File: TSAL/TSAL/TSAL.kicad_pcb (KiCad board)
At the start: 2 copper layers, 56.5 x 34.3 mm, 16 parts, among them J1 Conn_01x02, J2 Conn_01x02, J3 Conn_01x02, J4 Conn_01x02, Q1 Q_NMOS_GDS, U1 LTV-817S, U2 LM555xM

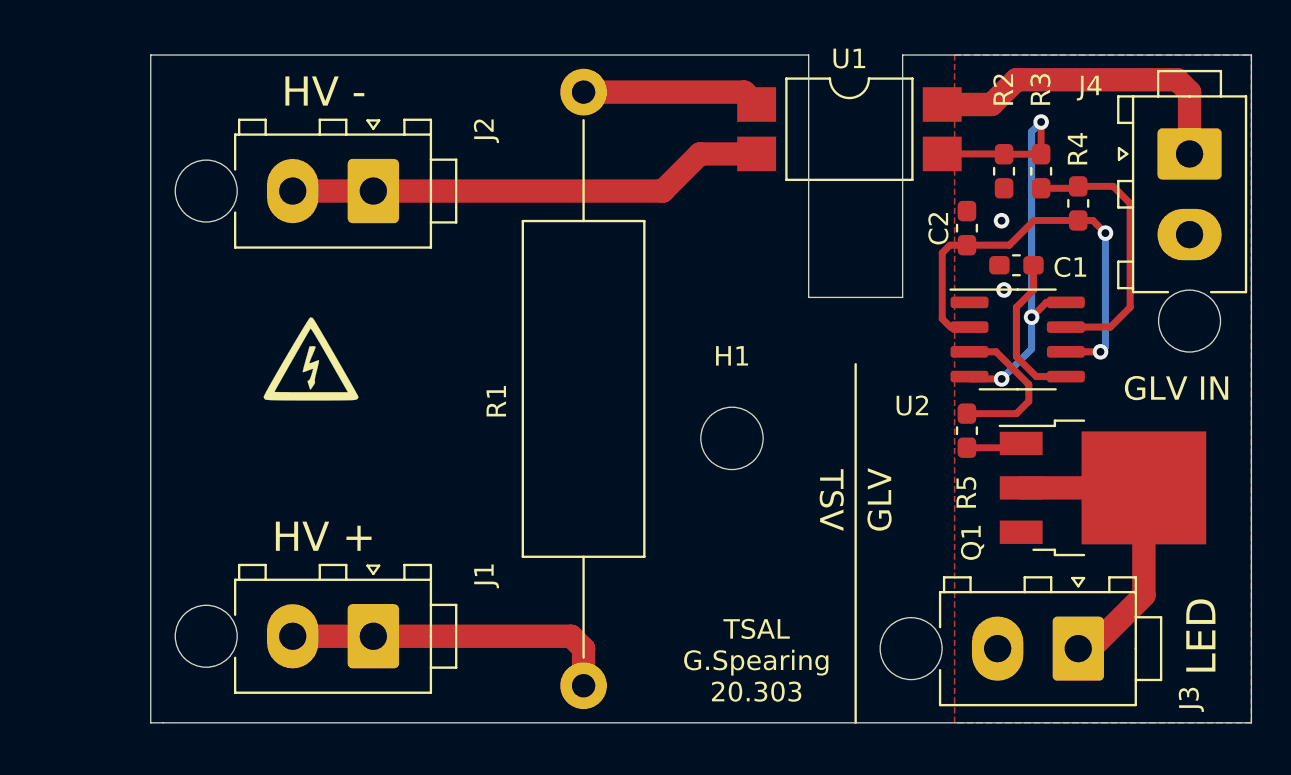
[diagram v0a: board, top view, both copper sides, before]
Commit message: change to CC driver
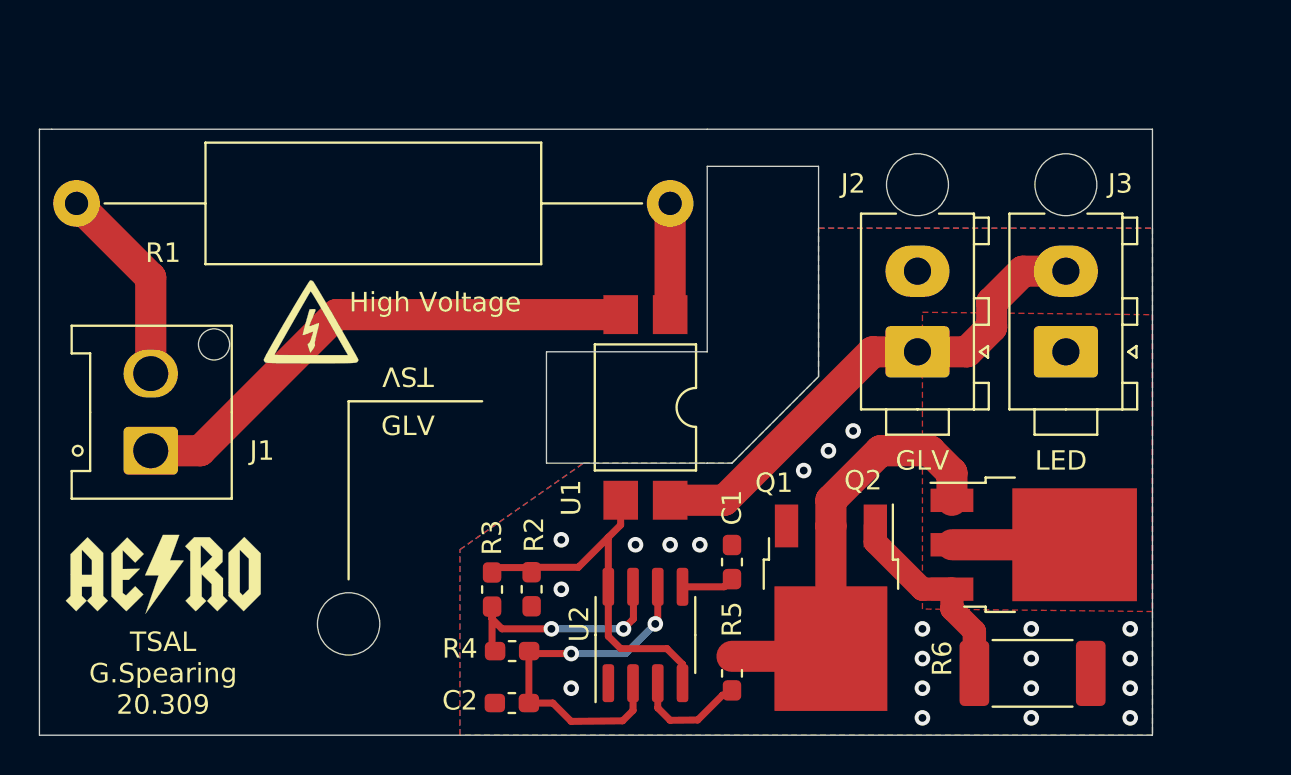
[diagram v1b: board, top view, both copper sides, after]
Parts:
- removed J4: Conn_01x02, Connector_TE-Connectivity:TE_MATE-N-LOK_1-770866-x_1x02_P4.14mm_Vertical
- added G***: LOGO, AERO_CUSTOM:AERO_Logo_10x4mm, F.Cu at (132.7, 90.2)
- added Q2: 040N03LG, Package_TO_SOT_SMD:TO-252-3_TabPin2, F.Cu at (177.4, 88.6)
- added R6: 0.75, Resistor_SMD:R_2512_6332Metric_Pad1.52x3.35mm_HandSolder, F.Cu at (177.4, 95.2)
- J1: footprint Connector_TE-Connectivity:TE_MATE-N-LOK_1-770866-x_1x02_P4.14mm_Vertical -> Connector_Hirose:Hirose_DF63R-2P-3.96DSA_1x02_P3.96mm_Vertical
- J2, J3: value Conn_01x02 -> 172165-1
- Q1: value Q_NMOS_GDS -> 040N03LG
- moved R4 37.1 mm to (150.6, 94.1), turned to 0 degrees
- moved R3 35.4 mm to (149.6, 90.9)
- moved C2 33.8 mm to (150.6, 96.8), turned to 180 degrees
- moved R2 32.4 mm to (151.6, 90.9)
- moved J2 29.1 mm to (171.4, 78.7), turned to 180 degrees
- moved U2 24.4 mm to (157.5, 93.3), turned to 90 degrees
- moved H1 21.9 mm to (142.2, 92.7)
- moved C1 21.1 mm to (161.9, 89.5), turned to 90 degrees
- moved U1 17.7 mm to (157.5, 81.6), turned to 270 degrees
- moved R5 17.3 mm to (161.9, 95.2), turned to 270 degrees
- moved Q1 15.3 mm to (167.0, 91.9), turned to 270 degrees
- moved J3 15.3 mm to (179.1, 78.7), turned to 180 degrees
- moved J1 14.9 mm to (132.1, 83.8), turned to 90 degrees
- moved R1 7.24 mm to (158.8, 71.1), turned to 180 degrees
- moved Ref** 1.91 mm to (140.3, 79.4)
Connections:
- net /LED_OUT renamed /555_OUT
- J1 pad 1: /HV+ -> /HV-
- J2 pad 1: /HV- -> +12V
- J2 pad 2: /HV- -> GND
- J3 pad 2: GND -> +12V
- Q1 pad 2: /RED_ON -> Net-(Q1-Pad2)
- R5 pad 1: Net-(Q1-Pad1) -> Net-(Q1-Pad2)
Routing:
- net Net-(Q1-Pad2): track 0.00 -> 22.0 mm
- net /RED_ON: track 16.3 -> 6.30 mm
- net +12V: track 17.3 -> 25.9 mm
- net Net-(Q1-Pad1): track 2.88 -> 10.6 mm
- net /HV+: track 17.1 -> 10.3 mm
- net Net-(C1-Pad1): track 8.02 -> 2.70 mm
- net VCC: track 24.6 -> 19.4 mm, vias 3 -> 0
- net Net-(R1-Pad1): track 9.15 -> 5.71 mm
- net /pass: track 22.3 -> 19.2 mm
- net /HV-: track 24.6 -> 27.0 mm
- net /555_OUT: track 8.04 -> 5.87 mm
- net Net-(R3-Pad2): track 14.0 -> 12.3 mm, vias 0 -> 2
- net GND: vias 2 -> 21
- added copper zone on F.Cu, net /RED_ON
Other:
- board size 56.5 x 34.3 mm -> 57.1 x 31.1 mm
- board text added: "High Voltage"
- board text added: "TSAL G.Spearing 20.309"
- board text removed: "GLV IN"
- board text removed: "HV +"
- board text removed: "HV -"
- board text removed: "TSAL G.Spearing 20.303"

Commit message: initial commit
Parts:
- removed G***: LOGO, AERO_CUSTOM:AERO_Logo_10x4mm
- removed Ref**: Val**, AERO_BOARD:hv_small
- added C3: 0.1u, Capacitor_SMD:C_0603_1608Metric_Pad1.05x0.95mm_HandSolder, F.Cu at (153.5, 89.2)
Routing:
- net GND: vias 21 -> 22

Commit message: TSAL Schematic and layout
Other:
- board text added: "HV+"
- board text added: "HV-"
